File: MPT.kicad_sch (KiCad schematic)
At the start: 6 parts, among them SW1 OS102011MA1QN1

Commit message: User Buttons Finished
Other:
- sheet User Buttons ports: added GPIO_BUTTON1, GPIO_BUTTON2, GPIO_BUTTON3, GPIO_BUTTON4, GPIO_BUTTON5, GPIO_JOYSTICK1, GPIO_JOYSTICK2, GPIO_JOYSTICK3, GPIO_JOYSTICK4, GPIO_JOYSTICK6; removed none
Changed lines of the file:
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@@
 	)
 	(sheet
-		(at 96.52 152.4)
-		(size 25.4 21.59)
+		(at 100.33 140.97)
+		(size 30.48 21.59)
 		(exclude_from_sim no)
 		(in_bom yes)
@@
 		)
 		(property "Sheetname" "User Buttons"
-			(at 96.52 151.6884 0)
+			(at 99.6184 162.56 90)
 			(show_name no)
 			(do_not_autoplace no)
@@
 		)
 		(property "Sheetfile" "mpt_user_buttons.kicad_sch"
-			(at 96.52 174.5746 0)
+			(at 131.3946 162.56 90)
 			(show_name no)
 			(do_not_autoplace no)
@@
 			)
 		)
+		(pin "GPIO_BUTTON1" output
+			(at 102.87 140.97 90)
+			(effects
+				(font
+					(size 1.27 1.27)
+				)
+				(justify right)
+			)
+		)
+		(pin "GPIO_BUTTON2" output
+			(at 105.41 140.97 90)
+			(effects
+				(font
+					(size 1.27 1.27)
+				)
+				(justify right)
+			)
+		)
+		(pin "GPIO_BUTTON3" output
+			(at 107.95 140.97 90)
+			(effects
+				(font
+					(size 1.27 1.27)
+				)
+				(justify right)
+			)
+		)
+		(pin "GPIO_BUTTON4" output
+			(at 110.49 140.97 90)
+			(effects
+				(font
+					(size 1.27 1.27)
+				)
+				(justify right)
+			)
+		)
+		(pin "GPIO_BUTTON5" output
+			(at 113.03 140.97 90)
+			(effects
+				(font
+					(size 1.27 1.27)
+				)
+				(justify right)
+			)
+		)
+		(pin "GPIO_JOYSTICK1" output
+			(at 116.84 140.97 90)
+			(effects
+				(font
+					(size 1.27 1.27)
+				)
+				(justify right)
+			)
+		)
+		(pin "GPIO_JOYSTICK2" output
+			(at 119.38 140.97 90)
+			(effects
+				(font
+					(size 1.27 1.27)
+				)
+				(justify right)
+			)
+		)
+		(pin "GPIO_JOYSTICK3" output
+			(at 121.92 140.97 90)
+			(effects
+				(font
+					(size 1.27 1.27)
+				)
+				(justify right)
+			)
+		)
+		(pin "GPIO_JOYSTICK4" output
+			(at 124.46 140.97 90)
+			(effects
+				(font
+					(size 1.27 1.27)
+				)
+				(justify right)
+			)
+		)
+		(pin "GPIO_JOYSTICK6" output
+			(at 127 140.97 90)
+			(effects
+				(font
+					(size 1.27 1.27)
+				)
+				(justify right)
+			)
+		)

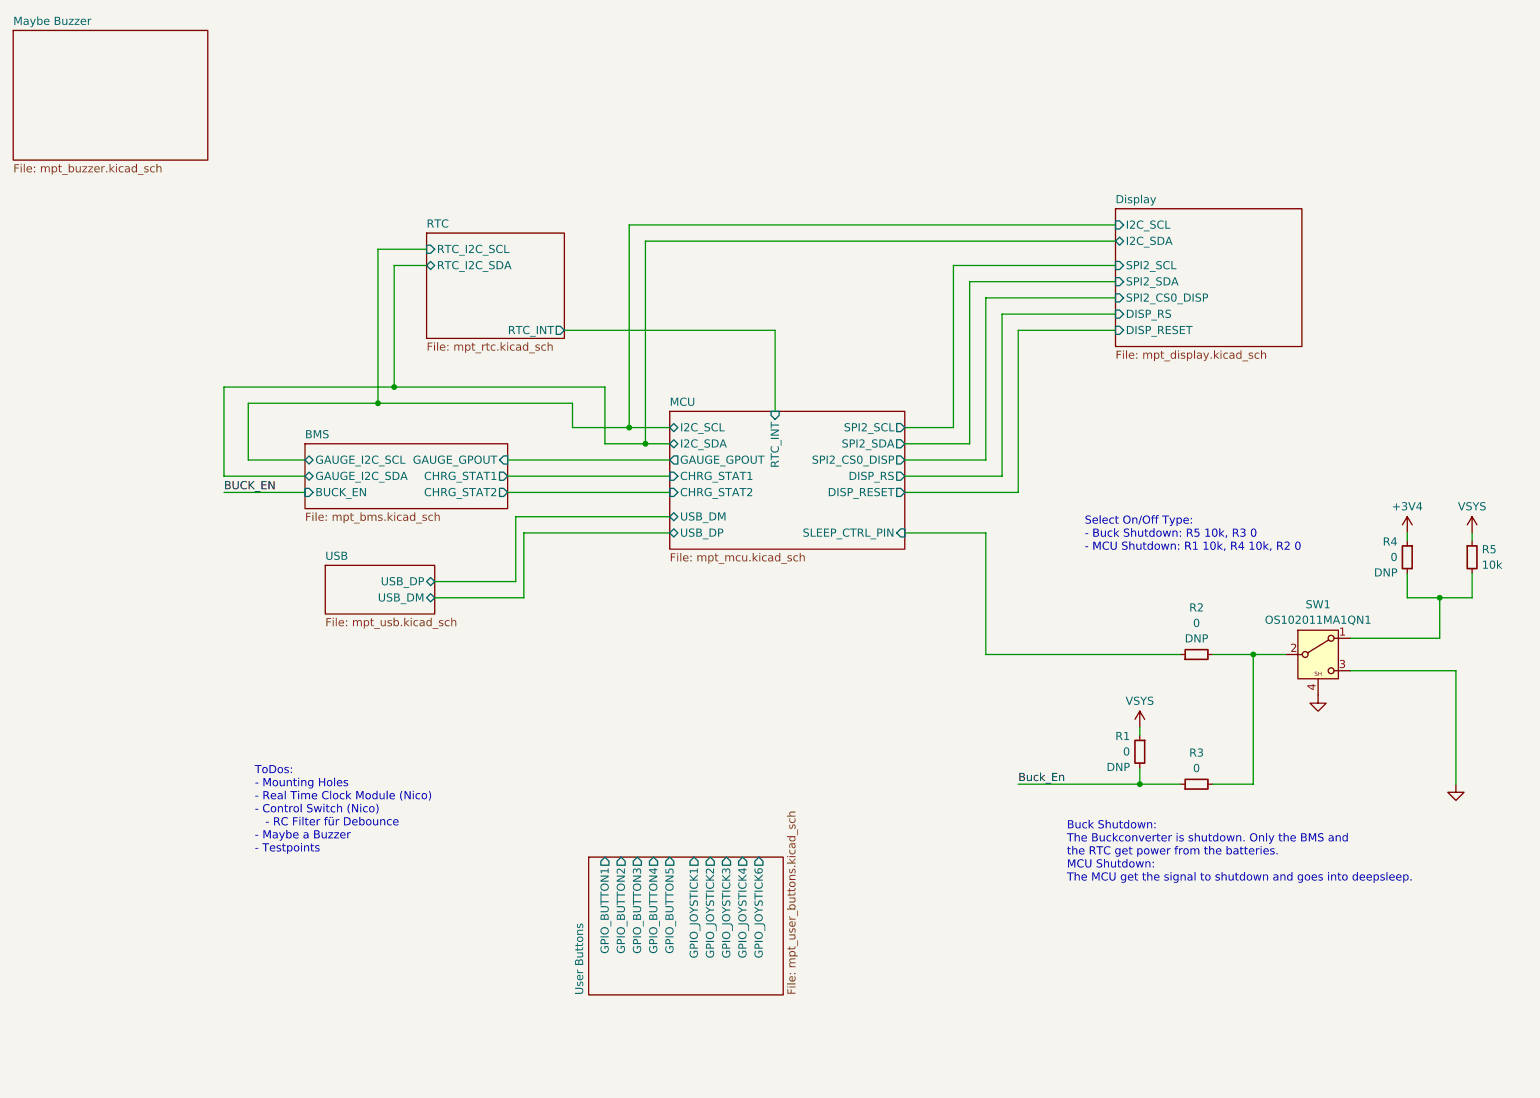
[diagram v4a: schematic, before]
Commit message: Updated PCB Layout with new Buck Boost, Display driver and STAT Led logic
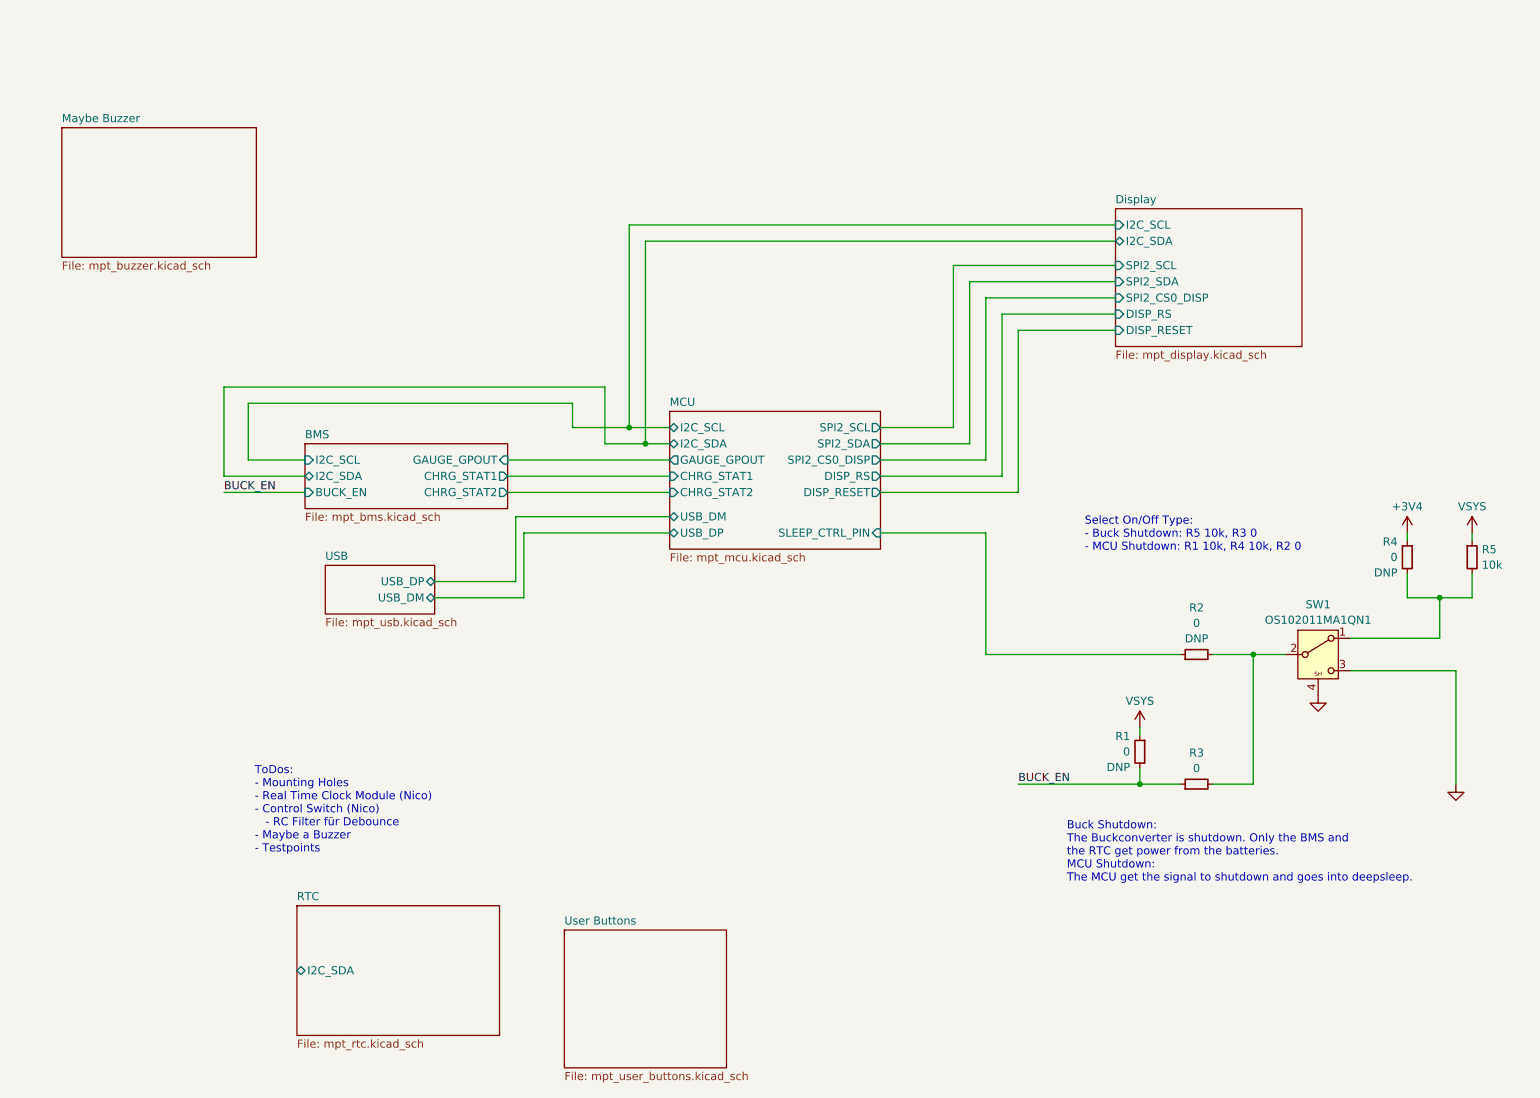
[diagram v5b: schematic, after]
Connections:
- net Buck_En is gone; now on net BUCK_EN: R1.2, R3.1
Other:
- sheet BMS ports: added I2C_SCL, I2C_SDA; removed GAUGE_I2C_SCL, GAUGE_I2C_SDA
- sheet MCU ports: added none; removed RTC_INT
- sheet RTC ports: added I2C_SDA; removed RTC_I2C_SCL, RTC_I2C_SDA, RTC_INT
- sheet User Buttons ports: added none; removed GPIO_BUTTON1, GPIO_BUTTON2, GPIO_BUTTON3, GPIO_BUTTON4, GPIO_BUTTON5, GPIO_JOYSTICK1, GPIO_JOYSTICK2, GPIO_JOYSTICK3, GPIO_JOYSTICK4, GPIO_JOYSTICK6

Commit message: Sleep Control Sub-Sheet created, Hirarchy Labels renamed connected
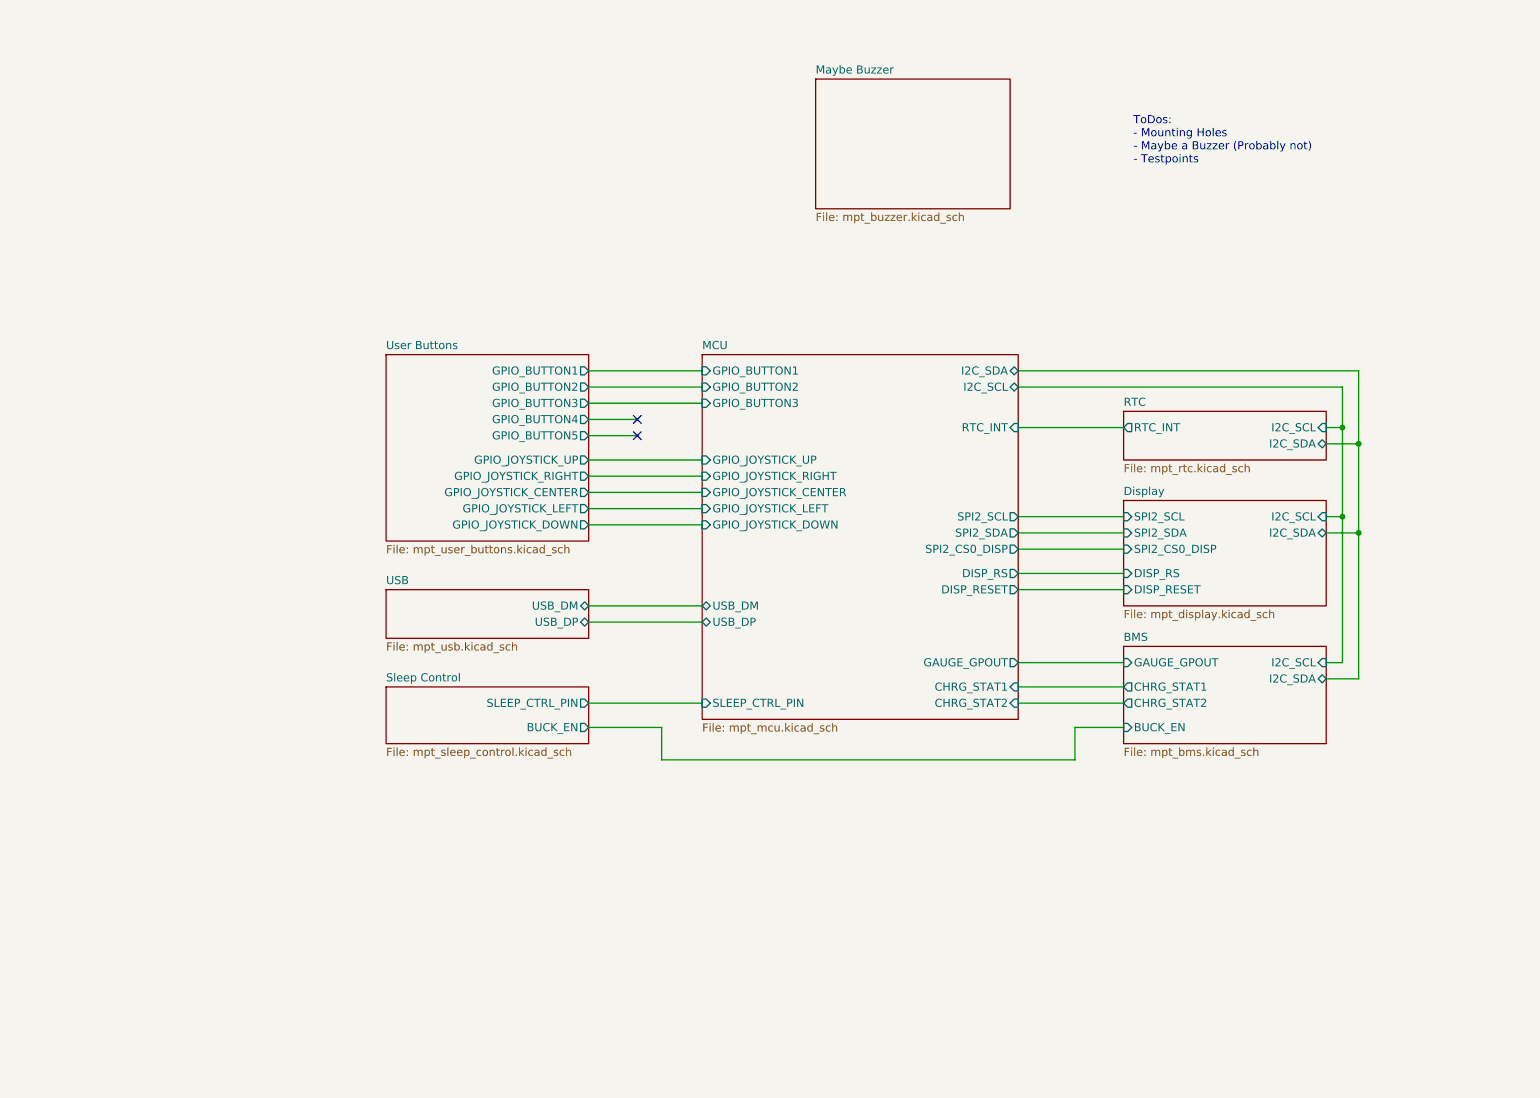
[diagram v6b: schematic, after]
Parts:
- removed R1, R2, R4: 0, passive:R_0603_DNP, symbol db:resistor/00.000.0000.0002
- removed R3: 0, passive:R_0603, symbol db:resistor_0603/00.000.0000.0001
- removed R5: 10k, passive:R_0603, symbol db:resistor_0603/00.018.0009.0046
- removed SW1: OS102011MA1QN1, switch:OS102011MA1QN1_CNK, symbol db:switch/06.004.0051.0001
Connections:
- no-connect marks 0 -> 2
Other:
- added sheet Sleep Control (mpt_sleep_control.kicad_sch)
- sheet MCU ports: added GPIO_BUTTON1, GPIO_BUTTON2, GPIO_BUTTON3, GPIO_JOYSTICK_CENTER, GPIO_JOYSTICK_DOWN, GPIO_JOYSTICK_LEFT, GPIO_JOYSTICK_RIGHT, GPIO_JOYSTICK_UP, RTC_INT; removed none
- sheet RTC ports: added I2C_SCL, RTC_INT; removed none
- sheet User Buttons ports: added GPIO_BUTTON1, GPIO_BUTTON2, GPIO_BUTTON3, GPIO_BUTTON4, GPIO_BUTTON5, GPIO_JOYSTICK_CENTER, GPIO_JOYSTICK_DOWN, GPIO_JOYSTICK_LEFT, GPIO_JOYSTICK_RIGHT, GPIO_JOYSTICK_UP; removed none
- note added: "ToDos: - Mounting Holes - Maybe a Buzzer (Probably not) - Testpoints"
- note removed: "Buck Shutdown: The Buckconverter is shutdown. Only the BMS and the RTC get power from the batteries. MCU Shutdown: The MCU get the signal to shutdown and goes into deepsleep."
- note removed: "Select On/Off Type: - Buck Shutdown: R5 10k, R3 0 - MCU Shutdown: R1 10k, R4 10k, R2 0"
- note removed: "ToDos: - Mounting Holes - Real Time Clock Module (Nico) - Control Switch (Nico) - RC Filter für Debounce - Maybe a Buzzer - Testpoints"

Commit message: Make Block Titles consistent in size Remove not connected marks on mcu for pins which can be used for user buttons and other stuff Add User button hierarchy lables for Button 4 & 5 on MCU sheet Fix hierarchichal pin names on the block not matching the sheet
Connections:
- no-connect marks 2 -> 0
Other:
- sheet MCU ports: added GPIO_BUTTON4, GPIO_BUTTON5; removed none
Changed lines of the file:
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@@
 		(color 0 0 0 0)
 	)
-	(no_connect
-		(at 107.95 72.39)
-	)
-	(no_connect
-		(at 107.95 74.93)
-	)
 	(wire
 		(pts
@@
 	(wire
 		(pts
-			(xy 100.33 72.39) (xy 107.95 72.39)
+			(xy 100.33 72.39) (xy 118.11 72.39)
 		)
 		(stroke
@@
 	(wire
 		(pts
-			(xy 100.33 74.93) (xy 107.95 74.93)
+			(xy 100.33 74.93) (xy 118.11 74.93)
 		)
 		(stroke
@@
 			)
 		)
+		(pin "GPIO_BUTTON4" input
+			(at 118.11 72.39 180)
+			(effects
+				(font
+					(size 1.27 1.27)
+				)
+				(justify left)
+			)
+		)
+		(pin "GPIO_BUTTON5" input
+			(at 118.11 74.93 180)
+			(effects
+				(font
+					(size 1.27 1.27)
+				)
+				(justify left)
+			)
+		)

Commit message: Footprints added, Userbuttons and RTC added on PCB Layout
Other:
- sheet MCU ports: added none; removed GPIO_BUTTON5
- sheet User Buttons ports: added none; removed GPIO_BUTTON5
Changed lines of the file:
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@@
-	(wire
-		(pts
-			(xy 100.33 74.93) (xy 118.11 74.93)
-		)
-		(stroke
-			(width 0)
-			(type default)
-		)
-	)
 	(wire
 		(pts
@@
 			)
 		)
-		(pin "GPIO_BUTTON5" output
-			(at 100.33 74.93 0)
-			(effects
-				(font
-					(size 1.27 1.27)
-				)
-				(justify right)
-			)
-		)
 		(pin "GPIO_JOYSTICK_CENTER" output
 			(at 100.33 83.82 0)
@@
 			(effects
 				(font
-					(size 1.27 1.27)
-				)
-				(justify left)
-			)
-		)
-		(pin "GPIO_BUTTON5" input
-			(at 118.11 74.93 180)
-			(effects
-				(font
